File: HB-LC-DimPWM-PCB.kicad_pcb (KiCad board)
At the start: 2 copper layers, 176.7 x 57.6 mm, 241 parts, among them J1 SWD, J2 12V Input, J3 Conn_01x05_Male, J4 Conn_01x05_Male, J5 Conn_01x05_Male, J6 Conn_01x05_Male, Q1 S9013, Q10 BSS84, Q11 2N7002, Q12 BSS84, Q13 VS5810AS, Q14 VS5810AS, Q15 VS5810AS, Q16 VS5810AS, Q17 S9013, Q18 S9013, Q19 S9013, Q2 BSS84, Q20 S9013, Q21 BSS84, Q22 2N7002, Q23 BSS84, Q24 2N7002, Q25 BSS84, Q26 2N7002, Q27 BSS84, Q28 2N7002, Q29 VS5810AS, Q3 2N7002, Q30 VS5810AS, Q31 VS5810AS, Q32 VS5810AS, Q33 S9013, Q34 S9013, Q35 S9013, Q36 S9013, Q37 BSS84, Q38 2N7002, Q39 BSS84, Q4 2N7002, Q40 2N7002, Q41 BSS84, Q42 2N7002, Q43 BSS84, Q44 2N7002, Q45 VS5810AS, Q46 VS5810AS, Q47 VS5810AS, Q48 VS5810AS, Q49 S9013, Q5 S9013, Q50 S9013, Q51 S9013, Q52 S9013, Q53 BSS84, Q54 2N7002, Q55 BSS84, Q56 2N7002, Q57 BSS84, Q58 2N7002, Q59 BSS84, Q6 S9013, Q60 2N7002, Q61 VS5810AS, Q62 VS5810AS, Q63 VS5810AS, Q64 VS5810AS, Q7 S9013, Q8 BSS84, Q9 2N7002, U1 STM32F103C8Tx, U2 AMS1117-3.3, U3 HomeMatic-sensor, Y1 8MHz

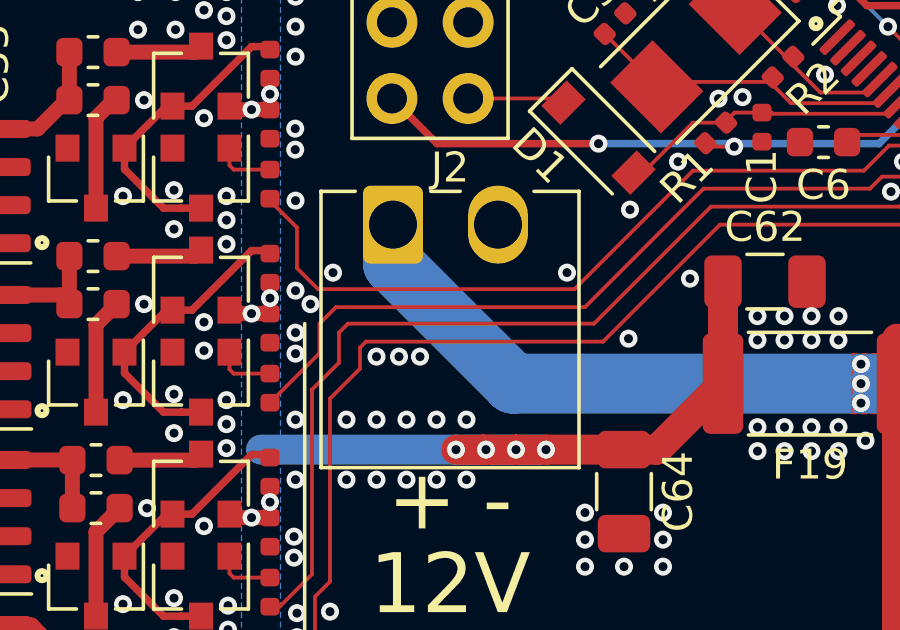
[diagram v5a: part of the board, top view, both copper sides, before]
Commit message: Add PWM channel designators
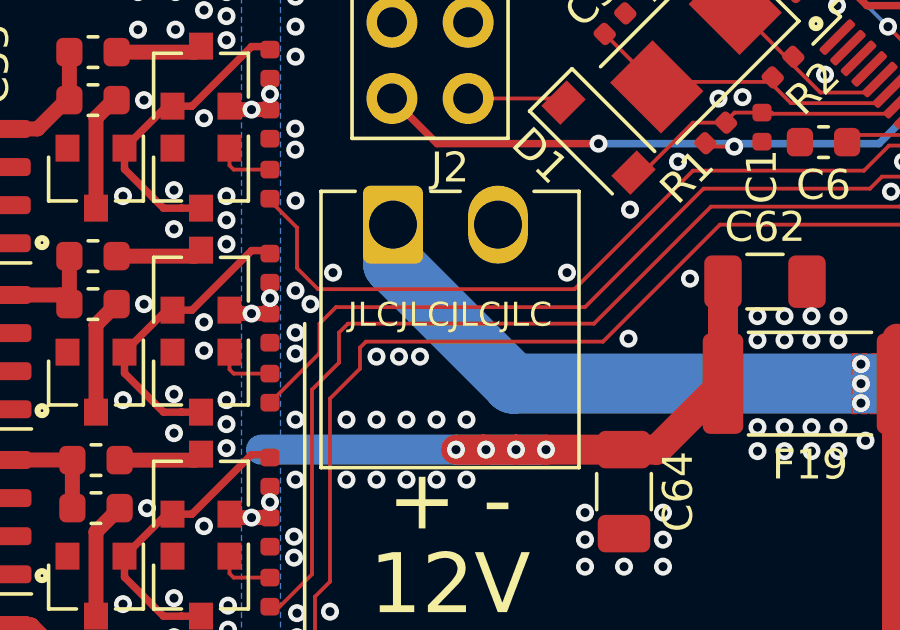
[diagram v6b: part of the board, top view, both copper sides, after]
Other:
- board text added: "JLCJLCJLCJLC"
- board text added: "PWM01"
- board text added: "PWM02"
- board text added: "PWM03"
- board text added: "PWM04"
- board text added: "PWM05"
- board text added: "PWM06"
- board text added: "PWM07"
- board text added: "PWM08"
- board text added: "PWM09"
- board text added: "PWM10"
- board text added: "PWM11"
- board text added: "PWM12"
- board text added: "PWM13"
- board text added: "PWM14"
- board text added: "PWM15"
- board text added: "PWM16"
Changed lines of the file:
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@@
   (general
     (thickness 1.6)
-    (drawings 31)
+    (drawings 52)
     (tracks 1653)
     (zones 0)
@@
     )
   )
+  (gr_text PWM13 (at 84.5 101.425) (layer B.SilkS)
+    (effects (font (size 1.5 1.5) (thickness 0.2)) (justify right mirror))
+  )
+  (gr_text PWM14 (at 84.5 104.825) (layer B.SilkS)
+    (effects (font (size 1.5 1.5) (thickness 0.2)) (justify right mirror))
+  )
+  (gr_text PWM16 (at 84.5 111.825) (layer B.SilkS)
+    (effects (font (size 1.5 1.5) (thickness 0.2)) (justify right mirror))
+  )
+  (gr_text PWM15 (at 84.5 108.325) (layer B.SilkS)
+    (effects (font (size 1.5 1.5) (thickness 0.2)) (justify right mirror))
+  )
+  (gr_text GND (at 84.5 97.825) (layer B.SilkS)
+    (effects (font (size 1.5 1.5) (thickness 0.2)) (justify right mirror))
+  )
+  (gr_text PWM12 (at 84.5 83.7) (layer B.SilkS)
+    (effects (font (size 1.5 1.5) (thickness 0.2)) (justify right mirror))
+  )
+  (gr_text PWM11 (at 84.5 80.2) (layer B.SilkS)
+    (effects (font (size 1.5 1.5) (thickness 0.2)) (justify right mirror))
+  )
+  (gr_text PWM10 (at 84.5 76.7) (layer B.SilkS)
+    (effects (font (size 1.5 1.5) (thickness 0.2)) (justify right mirror))
+  )
+  (gr_text PWM09 (at 84.5 73.3) (layer B.SilkS)
+    (effects (font (size 1.5 1.5) (thickness 0.2)) (justify right mirror))
+  )
+  (gr_text GND (at 84.5 69.7) (layer B.SilkS)
+    (effects (font (size 1.5 1.5) (thickness 0.2)) (justify right mirror))
+  )
+  (gr_text PWM06 (at 261.44 105.16) (layer B.SilkS)
+    (effects (font (size 1.5 1.5) (thickness 0.2)) (justify left mirror))
+  )
+  (gr_text PWM05 (at 261.44 108.66) (layer B.SilkS)
+    (effects (font (size 1.5 1.5) (thickness 0.2)) (justify left mirror))
+  )
+  (gr_text GND (at 261.34 112.26) (layer B.SilkS)
+    (effects (font (size 1.5 1.5) (thickness 0.2)) (justify left mirror))
+  )
+  (gr_text PWM08 (at 261.44 98.16) (layer B.SilkS)
+    (effects (font (size 1.5 1.5) (thickness 0.2)) (justify left mirror))
+  )
+  (gr_text PWM07 (at 261.44 101.66) (layer B.SilkS)
+    (effects (font (size 1.5 1.5) (thickness 0.2)) (justify left mirror))
+  )
+  (gr_text PWM04 (at 261.4 70) (layer B.SilkS)
+    (effects (font (size 1.5 1.5) (thickness 0.2)) (justify left mirror))
+  )
+  (gr_text PWM03 (at 261.4 73.5) (layer B.SilkS)
+    (effects (font (size 1.5 1.5) (thickness 0.2)) (justify left mirror))
+  )
+  (gr_text PWM02 (at 261.4 77) (layer B.SilkS)
+    (effects (font (size 1.5 1.5) (thickness 0.2)) (justify left mirror))
+  )
+  (gr_text PWM01 (at 261.4 80.5) (layer B.SilkS)
+    (effects (font (size 1.5 1.5) (thickness 0.2)) (justify left mirror))
+  )
+  (gr_text GND (at 261.3 84.1) (layer B.SilkS)
+    (effects (font (size 1.5 1.5) (thickness 0.2)) (justify left mirror))
+  )
+  (gr_text JLCJLCJLCJLC (at 155.1 101) (layer F.SilkS)
+    (effects (font (size 0.8 0.8) (thickness 0.15)))
+  )
   (gr_text "HB PWM dimmer Rev A\nTobias Mädel\nTobias Schramm 2020" (at 159.6 79.2) (layer F.SilkS)

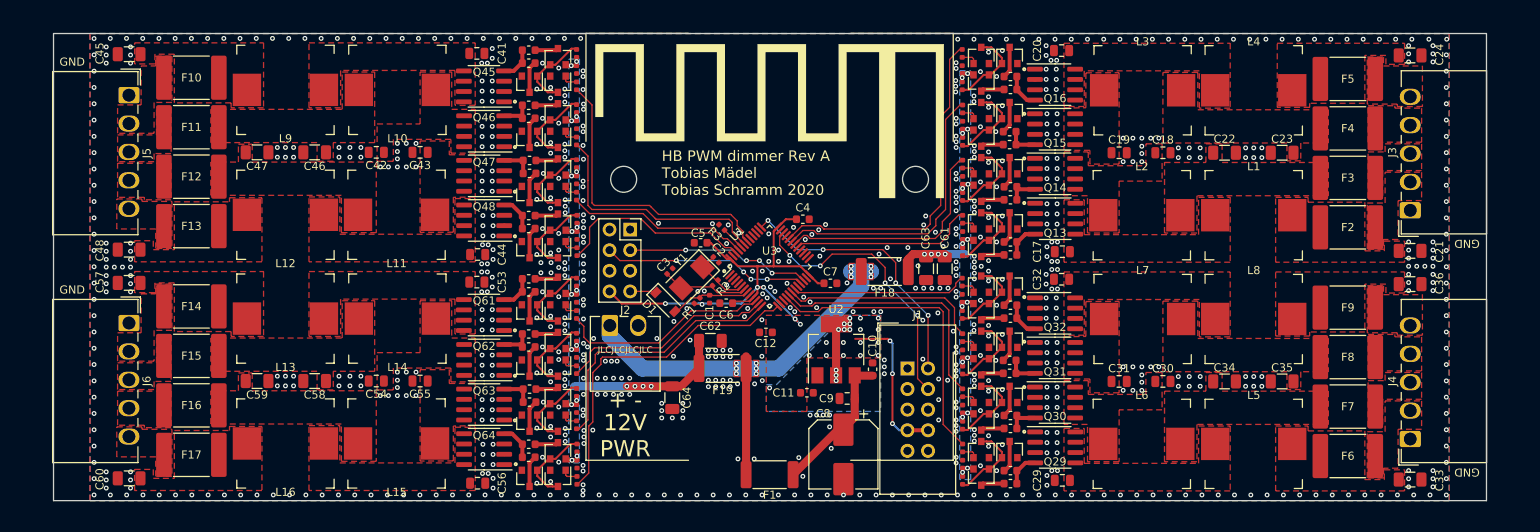
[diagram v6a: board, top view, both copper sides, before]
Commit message: Add tooling holes
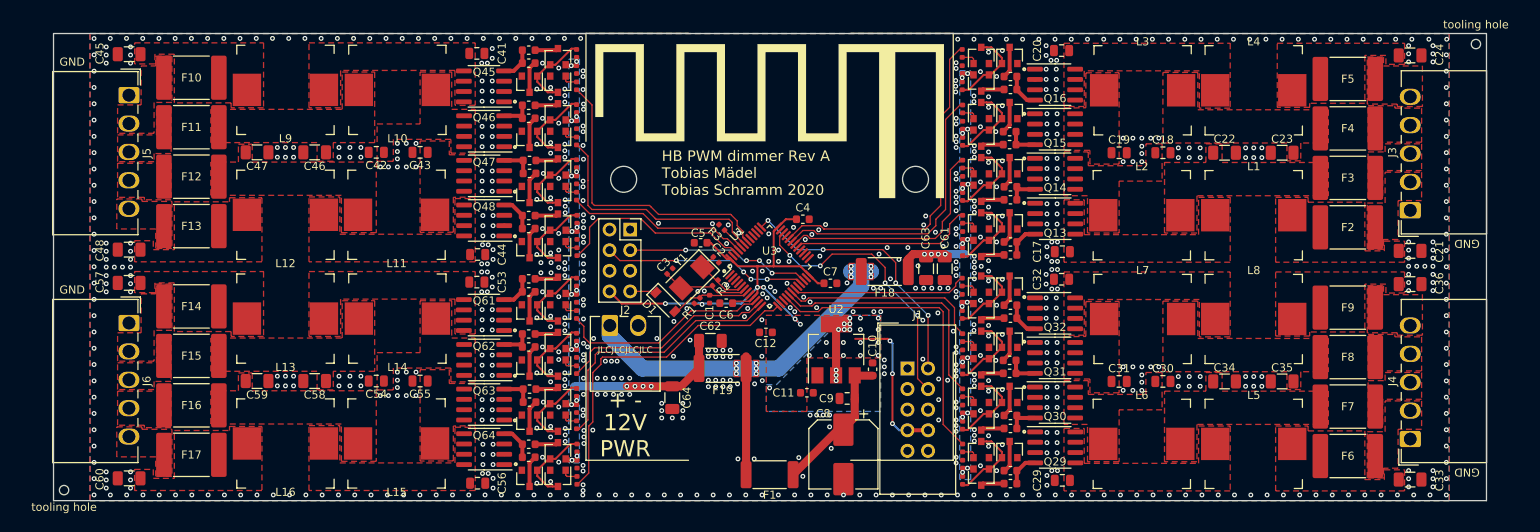
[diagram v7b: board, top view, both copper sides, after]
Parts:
- added H1: ToolingHole, ToolingHole:ToolingHole_JLCSMT, F.Cu at (85.9, 118.3)
- added H2: ToolingHole, ToolingHole:ToolingHole_JLCSMT, F.Cu at (260.0, 63.3)
